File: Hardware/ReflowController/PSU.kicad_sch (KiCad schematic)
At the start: 0 parts

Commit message: work on uC
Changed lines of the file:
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@@
 (kicad_sch (version 20211123) (generator eeschema)
   (paper "A4")
-  (hierarchical_label "N" (shape input) (at 125.73 93.98 0)
+  (hierarchical_label "24V_GND" (shape passive) (at 193.04 82.55 0)
     (effects (font (size 1.27 1.27)) (justify left))
   )
-  (hierarchical_label "24V_GND" (shape passive) (at 186.69 88.9 0)
+  (hierarchical_label "DGND" (shape passive) (at 193.04 91.44 0)
     (effects (font (size 1.27 1.27)) (justify left))
   )
-  (hierarchical_label "DGND" (shape passive) (at 186.69 97.79 0)
+  (hierarchical_label "24V_GND_IN" (shape passive) (at 142.24 82.55 0)
     (effects (font (size 1.27 1.27)) (justify left))
   )
-  (hierarchical_label "E" (shape tri_state) (at 125.73 96.52 0)
+  (hierarchical_label "+24V_IN" (shape input) (at 142.24 80.01 0)
     (effects (font (size 1.27 1.27)) (justify left))
   )
-  (hierarchical_label "L" (shape input) (at 125.73 91.44 0)
+  (hierarchical_label "+3.3VD" (shape output) (at 193.04 88.9 0)
     (effects (font (size 1.27 1.27)) (justify left))
   )
-  (hierarchical_label "+3.3VD" (shape output) (at 186.69 95.25 0)
+  (hierarchical_label "+5VD" (shape output) (at 193.04 86.36 0)
     (effects (font (size 1.27 1.27)) (justify left))
   )
-  (hierarchical_label "+5VD" (shape output) (at 186.69 92.71 0)
+  (hierarchical_label "+24V" (shape output) (at 193.04 78.74 0)
     (effects (font (size 1.27 1.27)) (justify left))
   )
-  (hierarchical_label "+24V" (shape output) (at 186.69 85.09 0)
-    (effects (font (size 1.27 1.27)) (justify left))
-  )

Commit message: defined rough structure with kerem
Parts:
- added U1: TSR_1-2450, Converter_DCDC:Converter_DCDC_TRACO_TSR-1_THT, symbol Regulator_Switching:TSR_1-2450
- added U2: LD1117S33TR_SOT223, Package_TO_SOT_SMD:SOT-223-3_TabPin2, symbol Regulator_Linear:LD1117S33TR_SOT223
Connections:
- net +24V_IN: now also U1.1 (Vin)
- net 24V_GND_IN: now also U1.2 (GND)
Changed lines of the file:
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@@
-(kicad_sch (version 20211123) (generator eeschema)
+(kicad_sch (version 20230121) (generator eeschema)
   (paper "A4")
-  (hierarchical_label "24V_GND" (shape passive) (at 193.04 82.55 0)
+  (wire (pts (xy 125.73 74.93) (xy 125.73 71.12))
+    (stroke (width 0) (type default))
+  )
+  (wire (pts (xy 97.79 63.5) (xy 115.57 63.5))
+    (stroke (width 0) (type default))
+  )
+  (wire (pts (xy 97.79 74.93) (xy 125.73 74.93))
+    (stroke (width 0) (type default))
+  )
+  (hierarchical_label "24V_GND" (shape passive) (at 193.04 82.55 0) (fields_autoplaced)
     (effects (font (size 1.27 1.27)) (justify left))
   )
-  (hierarchical_label "DGND" (shape passive) (at 193.04 91.44 0)
+  (hierarchical_label "DGND" (shape passive) (at 193.04 91.44 0) (fields_autoplaced)
     (effects (font (size 1.27 1.27)) (justify left))
   )
-  (hierarchical_label "24V_GND_IN" (shape passive) (at 142.24 82.55 0)
+  (hierarchical_label "24V_GND_IN" (shape passive) (at 97.79 74.93 180) (fields_autoplaced)
+    (effects (font (size 1.27 1.27)) (justify right))
+  )
+  (hierarchical_label "+24V_IN" (shape input) (at 97.79 63.5 180) (fields_autoplaced)
+    (effects (font (size 1.27 1.27)) (justify right))
+  )
+  (hierarchical_label "+3.3VD" (shape output) (at 193.04 88.9 0) (fields_autoplaced)
     (effects (font (size 1.27 1.27)) (justify left))
   )
-  (hierarchical_label "+24V_IN" (shape input) (at 142.24 80.01 0)
+  (hierarchical_label "+5VD" (shape output) (at 193.04 86.36 0) (fields_autoplaced)
     (effects (font (size 1.27 1.27)) (justify left))
   )
-  (hierarchical_label "+3.3VD" (shape output) (at 193.04 88.9 0)
+  (hierarchical_label "+24V" (shape output) (at 193.04 78.74 0) (fields_autoplaced)
     (effects (font (size 1.27 1.27)) (justify left))
   )
-  (hierarchical_label "+5VD" (shape output) (at 193.04 86.36 0)
-    (effects (font (size 1.27 1.27)) (justify left))
+  (symbol (lib_id "Regulator_Switching:TSR_1-2450") (at 125.73 66.04 0) (unit 1)
+    (in_bom yes) (on_board yes) (dnp no) (fields_autoplaced)
+    (property "Reference" "U1" (at 125.73 57.15 0)
+      (effects (font (size 1.27 1.27)))
+    )
+    (property "Value" "TSR_1-2450" (at 125.73 59.69 0)
+      (effects (font (size 1.27 1.27)))
+    )
+    (property "Footprint" "Converter_DCDC:Converter_DCDC_TRACO_TSR-1_THT" (at 125.73 69.85 0)
+      (effects (font (size 1.27 1.27) italic) (justify left) hide)
+    )
+    (property "Datasheet" "http://www.tracopower.com/products/tsr1.pdf" (at 125.73 66.04 0)
+      (effects (font (size 1.27 1.27)) hide)
+    )
+    (pin "1")
+    (pin "2")
+    (pin "3")
+    (instances
+      (project "ReflowController"
+        (path "/2394cc2a-b9b0-4c0b-be11-1fc6085b0d5c/f93d5910-f900-4b81-b729-10d58386d359"
+          (reference "U1") (unit 1)
+        )
+      )
+    )
   )
-  (hierarchical_label "+24V" (shape output) (at 193.04 78.74 0)
-    (effects (font (size 1.27 1.27)) (justify left))
+  (symbol (lib_id "Regulator_Linear:LD1117S33TR_SOT223") (at 127 93.98 0) (unit 1)
+    (in_bom yes) (on_board yes) (dnp no) (fields_autoplaced)
+    (property "Reference" "U2" (at 127 87.63 0)
+      (effects (font (size 1.27 1.27)))
+    )
+    (property "Value" "LD1117S33TR_SOT223" (at 127 90.17 0)
+      (effects (font (size 1.27 1.27)))
+    )
+    (property "Footprint" "Package_TO_SOT_SMD:SOT-223-3_TabPin2" (at 127 88.9 0)
+      (effects (font (size 1.27 1.27)) hide)
+    )
+    (property "Datasheet" "http://www.st.com/st-web-ui/static/active/en/resource/technical/document/datasheet/CD00000544.pdf" (at 129.54 100.33 0)
+      (effects (font (size 1.27 1.27)) hide)
+    )
+    (pin "1")
+    (pin "2")
+    (pin "3")
+    (instances
+      (project "ReflowController"
+        (path "/2394cc2a-b9b0-4c0b-be11-1fc6085b0d5c/f93d5910-f900-4b81-b729-10d58386d359"
+          (reference "U2") (unit 1)
+        )
+      )
+    )
   )
 )

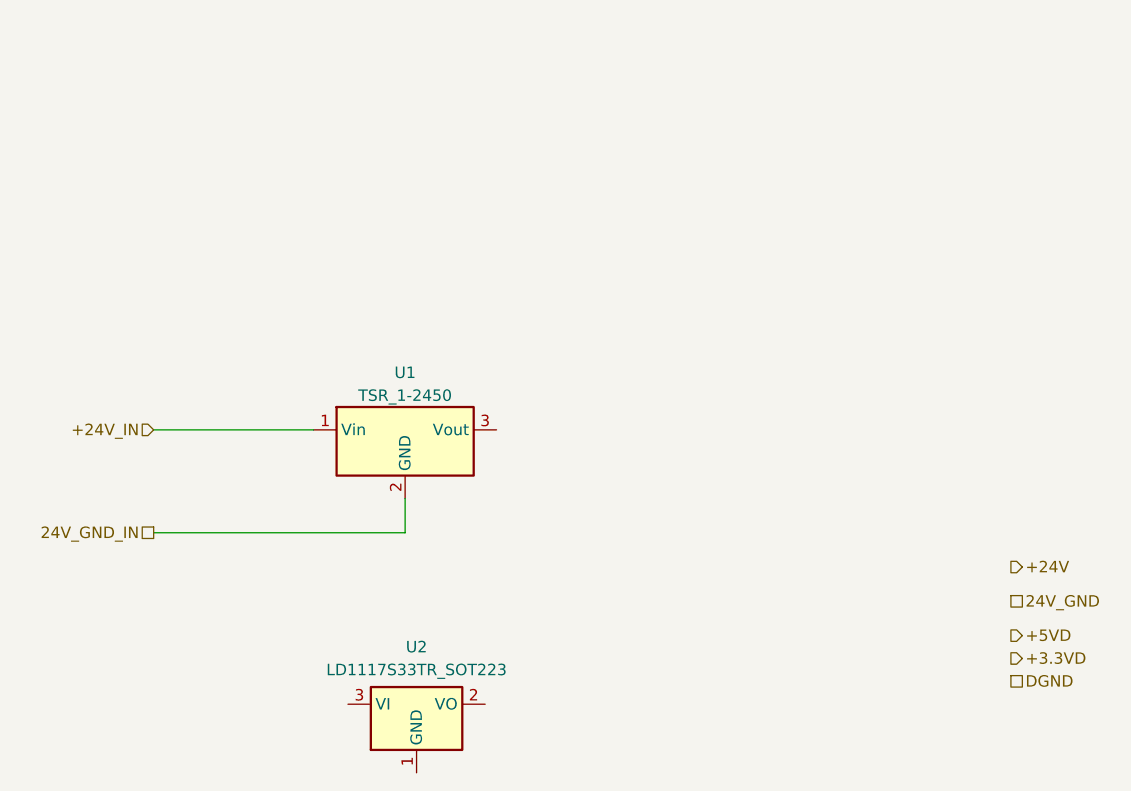
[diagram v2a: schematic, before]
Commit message: Finished the fan controllers calculations, added the wago connectors, added notes
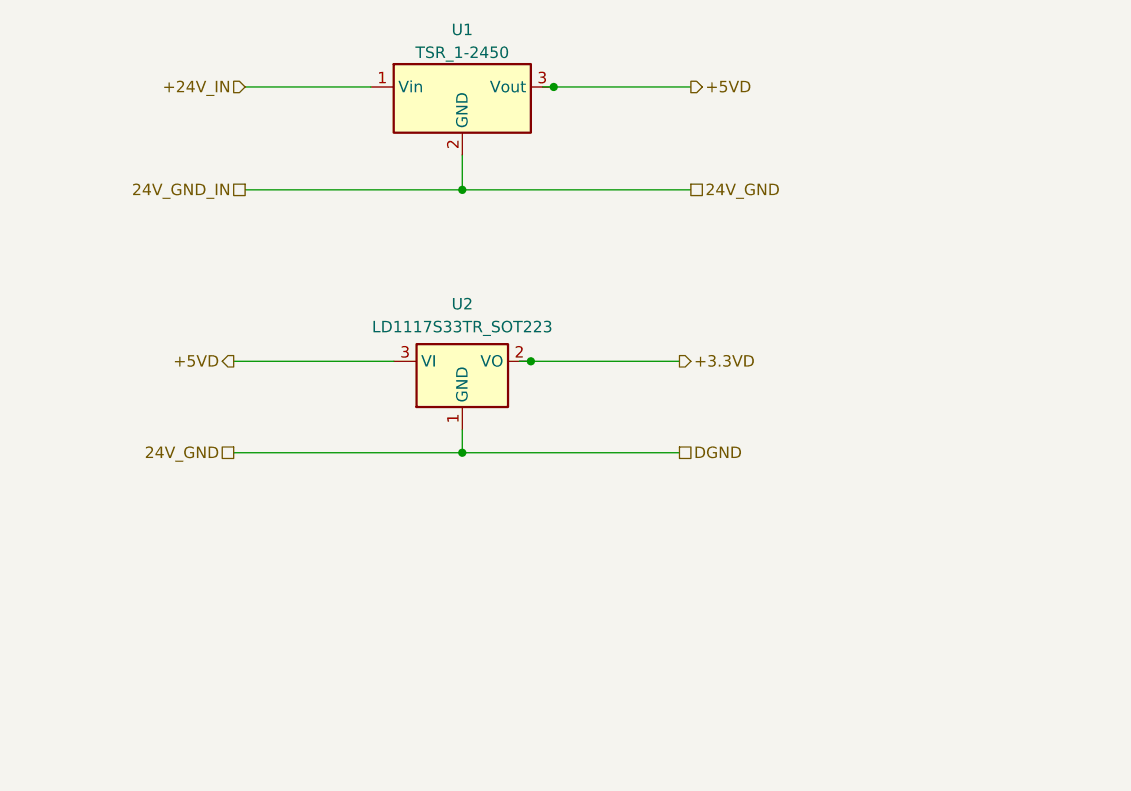
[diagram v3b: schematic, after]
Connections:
- net 24V_GND_IN is gone; now on net 24V_GND: U1.2 (GND)
- net +3.3VD: now also U2.2 (VO)
- net +5VD: now also U1.3 (Vout), U2.3 (VI)
- net 24V_GND: now also U2.1 (GND)
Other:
- title: (none) -> Reflow Oven Control
- moved on the sheet: U1, U2
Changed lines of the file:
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@@
 (kicad_sch (version 20230121) (generator eeschema)
   (paper "A4")
-  (wire (pts (xy 125.73 74.93) (xy 125.73 71.12))
+  (title_block
+    (title "Reflow Oven Control")
+    (date "2023-04-14")
+    (rev "0")
+  )
+  (junction (at 139.7 55.88) (diameter 0) (color 0 0 0 0)
+  )
+  (junction (at 132.08 66.04) (diameter 0) (color 0 0 0 0)
+  )
+  (junction (at 132.08 36.83) (diameter 0) (color 0 0 0 0)
+  )
+  (junction (at 142.24 25.4) (diameter 0) (color 0 0 0 0)
+  )
+  (wire (pts (xy 157.48 36.83) (xy 132.08 36.83))
     (stroke (width 0) (type default))
   )
-  (wire (pts (xy 97.79 63.5) (xy 115.57 63.5))
+  (wire (pts (xy 106.68 66.04) (xy 132.08 66.04))
     (stroke (width 0) (type default))
   )
-  (wire (pts (xy 97.79 74.93) (xy 125.73 74.93))
+  (wire (pts (xy 156.21 66.04) (xy 132.08 66.04))
     (stroke (width 0) (type default))
   )
-  (hierarchical_label "24V_GND" (shape passive) (at 193.04 82.55 0) (fields_autoplaced)
+  (wire (pts (xy 107.95 36.83) (xy 132.08 36.83))
+    (stroke (width 0) (type default))
+  )
+  (wire (pts (xy 106.68 55.88) (xy 124.46 55.88))
+    (stroke (width 0) (type default))
+  )
+  (wire (pts (xy 132.08 36.83) (xy 132.08 33.02))
+    (stroke (width 0) (type default))
+  )
+  (wire (pts (xy 132.08 66.04) (xy 132.08 63.5))
+    (stroke (width 0) (type default))
+  )
+  (wire (pts (xy 107.95 25.4) (xy 121.92 25.4))
+    (stroke (width 0) (type default))
+  )
+  (wire (pts (xy 142.24 25.4) (xy 157.48 25.4))
+    (stroke (width 0) (type default))
+  )
+  (wire (pts (xy 140.97 25.4) (xy 142.24 25.4))
+    (stroke (width 0) (type default))
+  )
+  (wire (pts (xy 139.7 55.88) (xy 156.21 55.88))
+    (stroke (width 0) (type default))
+  )
+  (wire (pts (xy 138.43 55.88) (xy 139.7 55.88))
+    (stroke (width 0) (type default))
+  )
+  (hierarchical_label "+5VD" (shape output) (at 106.68 55.88 180) (fields_autoplaced)
+    (effects (font (size 1.27 1.27)) (justify right))
+  )
+  (hierarchical_label "24V_GND" (shape passive) (at 106.68 66.04 180) (fields_autoplaced)
+    (effects (font (size 1.27 1.27)) (justify right))
+  )
+  (hierarchical_label "24V_GND" (shape passive) (at 157.48 36.83 0) (fields_autoplaced)
     (effects (font (size 1.27 1.27)) (justify left))
   )
-  (hierarchical_label "DGND" (shape passive) (at 193.04 91.44 0) (fields_autoplaced)
+  (hierarchical_label "24V_GND_IN" (shape passive) (at 107.95 36.83 180) (fields_autoplaced)
+    (effects (font (size 1.27 1.27)) (justify right))
+  )
+  (hierarchical_label "DGND" (shape passive) (at 156.21 66.04 0) (fields_autoplaced)
     (effects (font (size 1.27 1.27)) (justify left))
   )
-  (hierarchical_label "24V_GND_IN" (shape passive) (at 97.79 74.93 180) (fields_autoplaced)
+  (hierarchical_label "+3.3VD" (shape output) (at 156.21 55.88 0) (fields_autoplaced)
+    (effects (font (size 1.27 1.27)) (justify left))
+  )
+  (hierarchical_label "+24V_IN" (shape input) (at 107.95 25.4 180) (fields_autoplaced)
     (effects (font (size 1.27 1.27)) (justify right))
   )
-  (hierarchical_label "+24V_IN" (shape input) (at 97.79 63.5 180) (fields_autoplaced)
-    (effects (font (size 1.27 1.27)) (justify right))
-  )
-  (hierarchical_label "+3.3VD" (shape output) (at 193.04 88.9 0) (fields_autoplaced)
+  (hierarchical_label "+5VD" (shape output) (at 157.48 25.4 0) (fields_autoplaced)
     (effects (font (size 1.27 1.27)) (justify left))
   )
-  (hierarchical_label "+5VD" (shape output) (at 193.04 86.36 0) (fields_autoplaced)
-    (effects (font (size 1.27 1.27)) (justify left))
-  )
-  (hierarchical_label "+24V" (shape output) (at 193.04 78.74 0) (fields_autoplaced)
-    (effects (font (size 1.27 1.27)) (justify left))
-  )
-  (symbol (lib_id "Regulator_Switching:TSR_1-2450") (at 125.73 66.04 0) (unit 1)
+  (symbol (lib_id "Regulator_Switching:TSR_1-2450") (at 132.08 27.94 0) (unit 1)
     (in_bom yes) (on_board yes) (dnp no) (fields_autoplaced)
-    (property "Reference" "U1" (at 125.73 57.15 0)
+    (property "Reference" "U1" (at 132.08 19.05 0)
       (effects (font (size 1.27 1.27)))
     )
-    (property "Value" "TSR_1-2450" (at 125.73 59.69 0)
+    (property "Value" "TSR_1-2450" (at 132.08 21.59 0)
       (effects (font (size 1.27 1.27)))
     )
-    (property "Footprint" "Converter_DCDC:Converter_DCDC_TRACO_TSR-1_THT" (at 125.73 69.85 0)
+    (property "Footprint" "Converter_DCDC:Converter_DCDC_TRACO_TSR-1_THT" (at 132.08 31.75 0)
       (effects (font (size 1.27 1.27) italic) (justify left) hide)
     )
-    (property "Datasheet" "http://www.tracopower.com/products/tsr1.pdf" (at 125.73 66.04 0)
+    (property "Datasheet" "http://www.tracopower.com/products/tsr1.pdf" (at 132.08 27.94 0)
       (effects (font (size 1.27 1.27)) hide)
     )
@@
     )
   )
-  (symbol (lib_id "Regulator_Linear:LD1117S33TR_SOT223") (at 127 93.98 0) (unit 1)
+  (symbol (lib_id "Regulator_Linear:LD1117S33TR_SOT223") (at 132.08 55.88 0) (unit 1)
     (in_bom yes) (on_board yes) (dnp no) (fields_autoplaced)
-    (property "Reference" "U2" (at 127 87.63 0)
+    (property "Reference" "U2" (at 132.08 49.53 0)
       (effects (font (size 1.27 1.27)))
     )
-    (property "Value" "LD1117S33TR_SOT223" (at 127 90.17 0)
+    (property "Value" "LD1117S33TR_SOT223" (at 132.08 52.07 0)
       (effects (font (size 1.27 1.27)))
     )
-    (property "Footprint" "Package_TO_SOT_SMD:SOT-223-3_TabPin2" (at 127 88.9 0)
+    (property "Footprint" "Package_TO_SOT_SMD:SOT-223-3_TabPin2" (at 132.08 50.8 0)
       (effects (font (size 1.27 1.27)) hide)
     )
-    (property "Datasheet" "http://www.st.com/st-web-ui/static/active/en/resource/technical/document/datasheet/CD00000544.pdf" (at 129.54 100.33 0)
+    (property "Datasheet" "http://www.st.com/st-web-ui/static/active/en/resource/technical/document/datasheet/CD00000544.pdf" (at 134.62 62.23 0)
       (effects (font (size 1.27 1.27)) hide)
     )
